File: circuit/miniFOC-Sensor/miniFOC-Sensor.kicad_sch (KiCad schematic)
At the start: 6 parts, among them J1 Conn_01x05, U1 MT6701, U2 XC6206P332MR

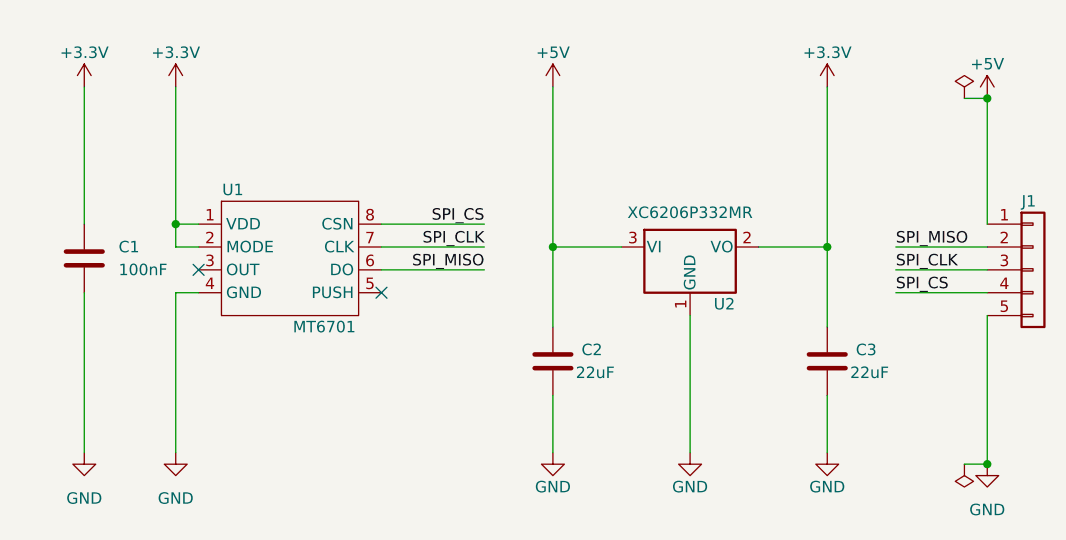
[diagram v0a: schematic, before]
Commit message: Updated the version number of the sensor board and adjusted the silk screen position in the PCB.
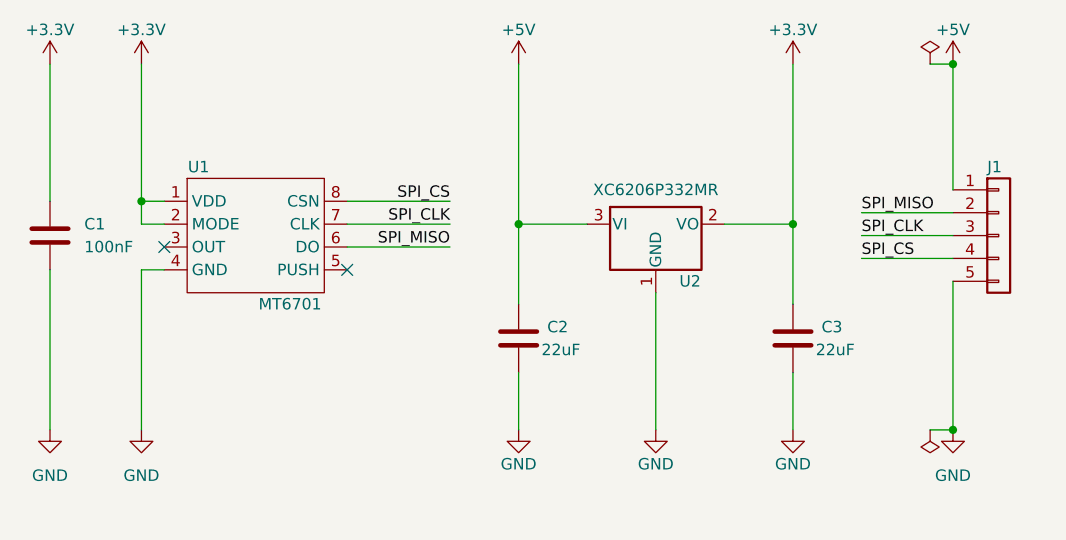
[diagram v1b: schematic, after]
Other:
- moved on the sheet: C1, C2, C3, J1, U1, U2
